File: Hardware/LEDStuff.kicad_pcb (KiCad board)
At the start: 2 copper layers, 41.9 x 56.2 mm, 24 parts, among them J1 Barrel_Jack, J2 AVR-ISP-6, J3 Conn_01x04_Male, Q1 Q_NMOS_GSD, Q2 Q_NMOS_GSD, Q3 Q_NMOS_GSD, U1 ATMEGA328P-AU, U2 LM7805_TO220, Y1 16MHz

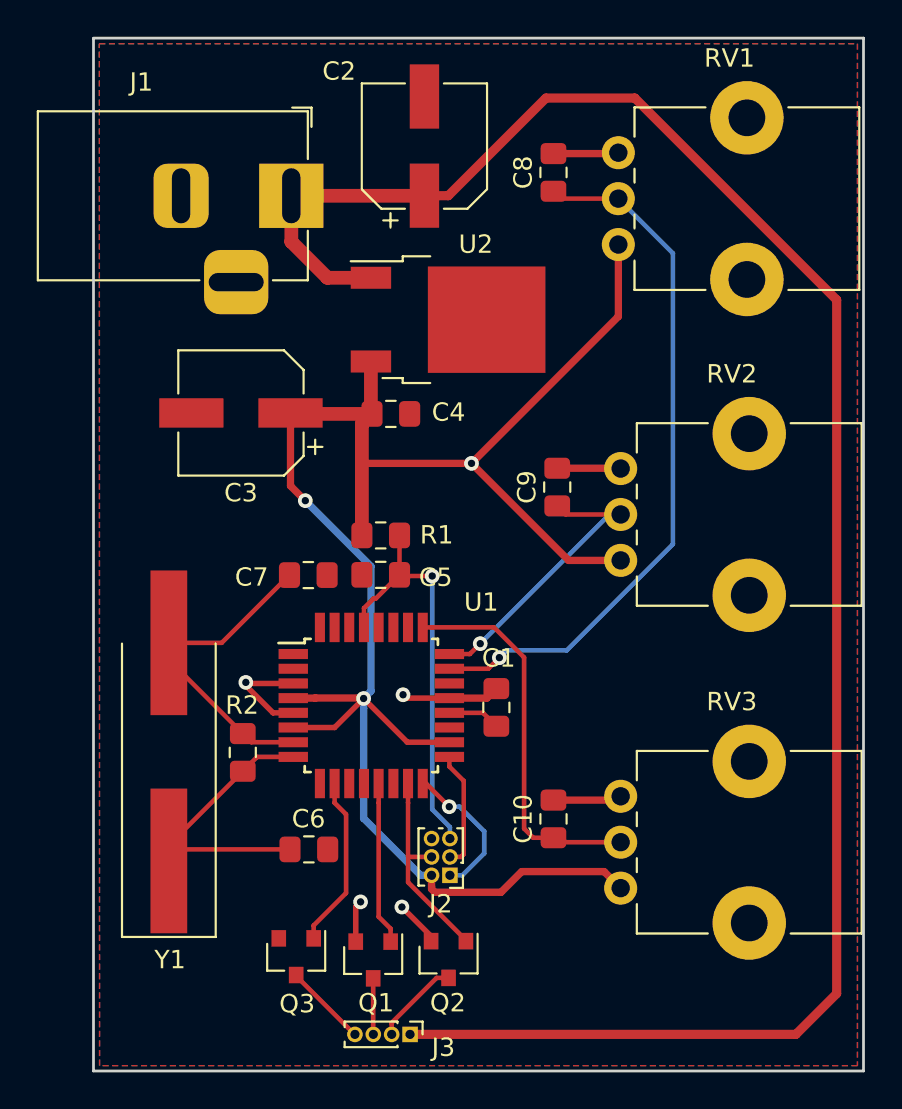
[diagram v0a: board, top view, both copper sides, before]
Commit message: board v2 add UART pins, 3.3V to 5V level shifter, change headers to standard 0.1" pin pitch
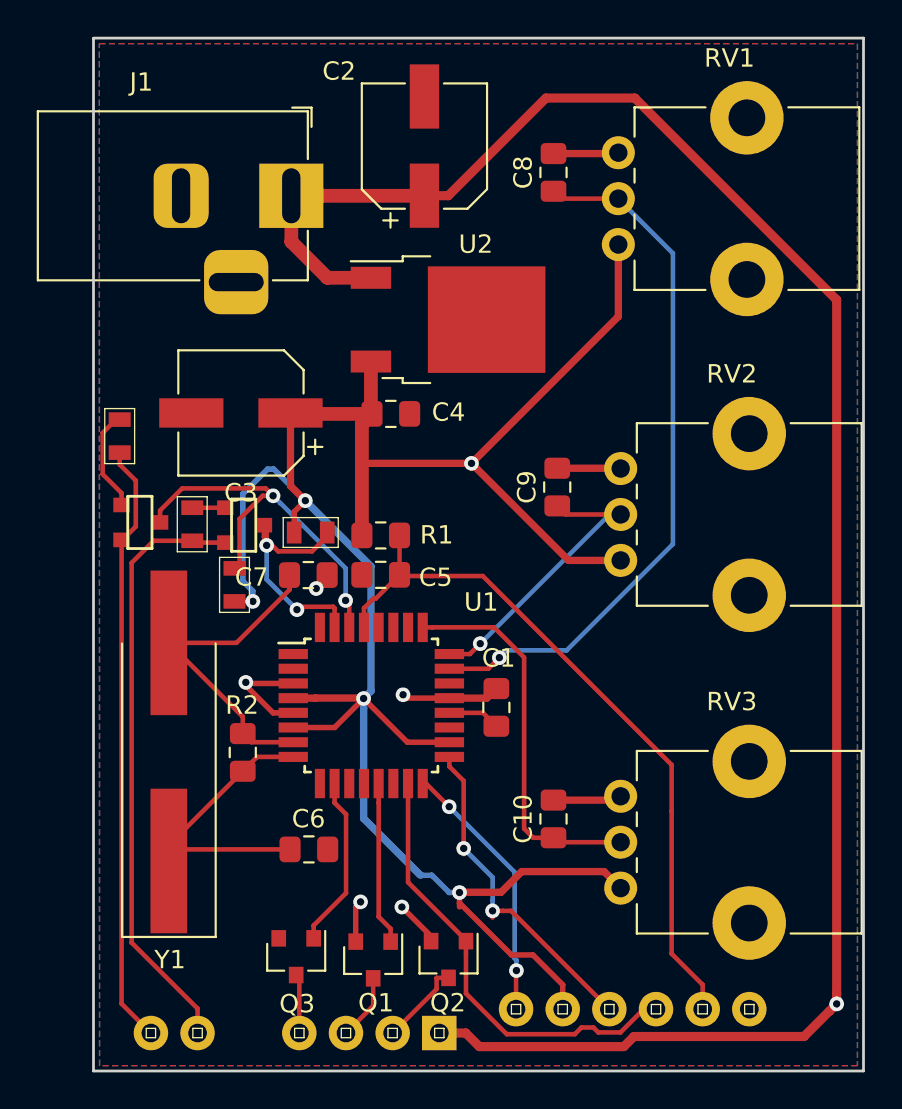
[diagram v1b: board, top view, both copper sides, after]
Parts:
- added J4: UART, SparkFun-Connectors:1X02, F.Cu at (134.0, 121.3)
- added Q4: MOSFET-NCHANNELBSS138, SparkFun-DigitalIC:SOT23-3, F.Cu at (133.4, 93.5)
- added Q5: MOSFET-NCHANNELBSS138, SparkFun-DigitalIC:SOT23-3, F.Cu at (139.1, 93.7)
- added R3: R, SparkFun-Resistors:0805, F.Cu at (142.7, 94.0)
- added R4: R, SparkFun-Resistors:0805, F.Cu at (138.6, 96.9)
- added R5: R, SparkFun-Resistors:0805, F.Cu at (136.2, 93.6)
- added R6: R, SparkFun-Resistors:0805, F.Cu at (132.3, 88.8)
- J2: footprint Connector_PinHeader_1.00mm:PinHeader_2x03_P1.00mm_Vertical -> SparkFun-Connectors:1X06
- J3: footprint Connector_PinHeader_1.00mm:PinHeader_1x04_P1.00mm_Vertical -> SparkFun-Connectors:1X04
- moved J2 8.13 mm to (153.9, 120.0), turned to 0 degrees
- moved J3 1.59 mm to (149.7, 121.3), turned to 180 degrees
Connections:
- net Net-(C6-Pad1) renamed /XTAL2
- net Net-(C7-Pad1) renamed /XTAL1
- U1 pad 30: Net-(U1-Pad30) -> /RXD
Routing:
- net /UART_RX_LEVELSHIFTED: track 0.00 -> 33.0 mm
- net /UART_TX_LEVELSHIFTED: track 0.00 -> 32.7 mm
- net +5V: track 100.7 -> 123.6 mm, vias 3 -> 5
- net /RXD: track 0.00 -> 21.5 mm, vias 0 -> 2
- net /RESET: track 22.4 -> 39.0 mm, vias 1 -> 0
- net /GREEN_PWM_OUT: track 11.2 -> 24.8 mm
- net Net-(Q5-Pad3): track 0.00 -> 13.5 mm, vias 0 -> 2
- net /SCK: track 6.43 -> 18.6 mm, vias 0 -> 2
- net /MISO: track 7.99 -> 14.5 mm, vias 1 -> 2
- net Net-(Q4-Pad1): track 0.00 -> 5.57 mm
- net Net-(Q5-Pad1): track 0.00 -> 1.80 mm
- net /BLUE_LED_OUT: track 4.56 -> 3.28 mm
- net GND: track 26.9 -> 27.9 mm, vias 4 -> 5
- net /XTAL1: track 17.6 -> 18.6 mm
- net +12V: track 106.0 -> 105.3 mm, vias 0 -> 1
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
